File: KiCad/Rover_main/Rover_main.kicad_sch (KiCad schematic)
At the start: 50 parts, among them J1 ToF sensor header, J2 12v Regulator, J3 40 pin Nano header, J4 Motor 2, J5 Motor 1, J6 Motor 3, J7 Motor 4

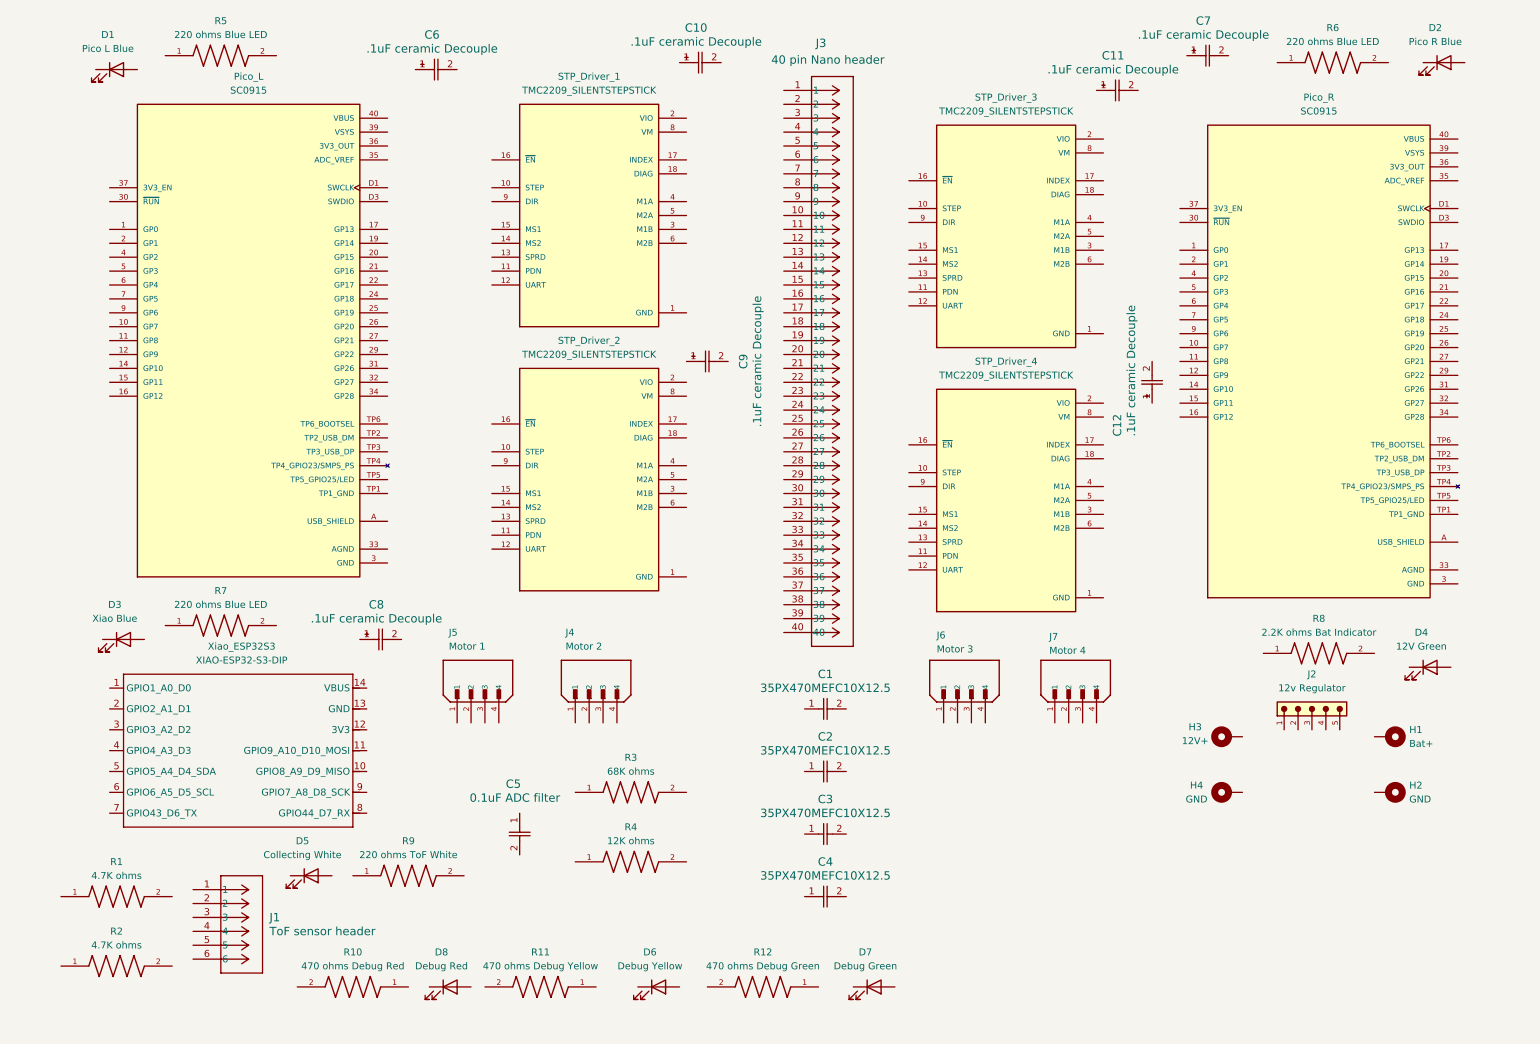
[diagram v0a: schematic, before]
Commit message: Updated KiCad Schematic
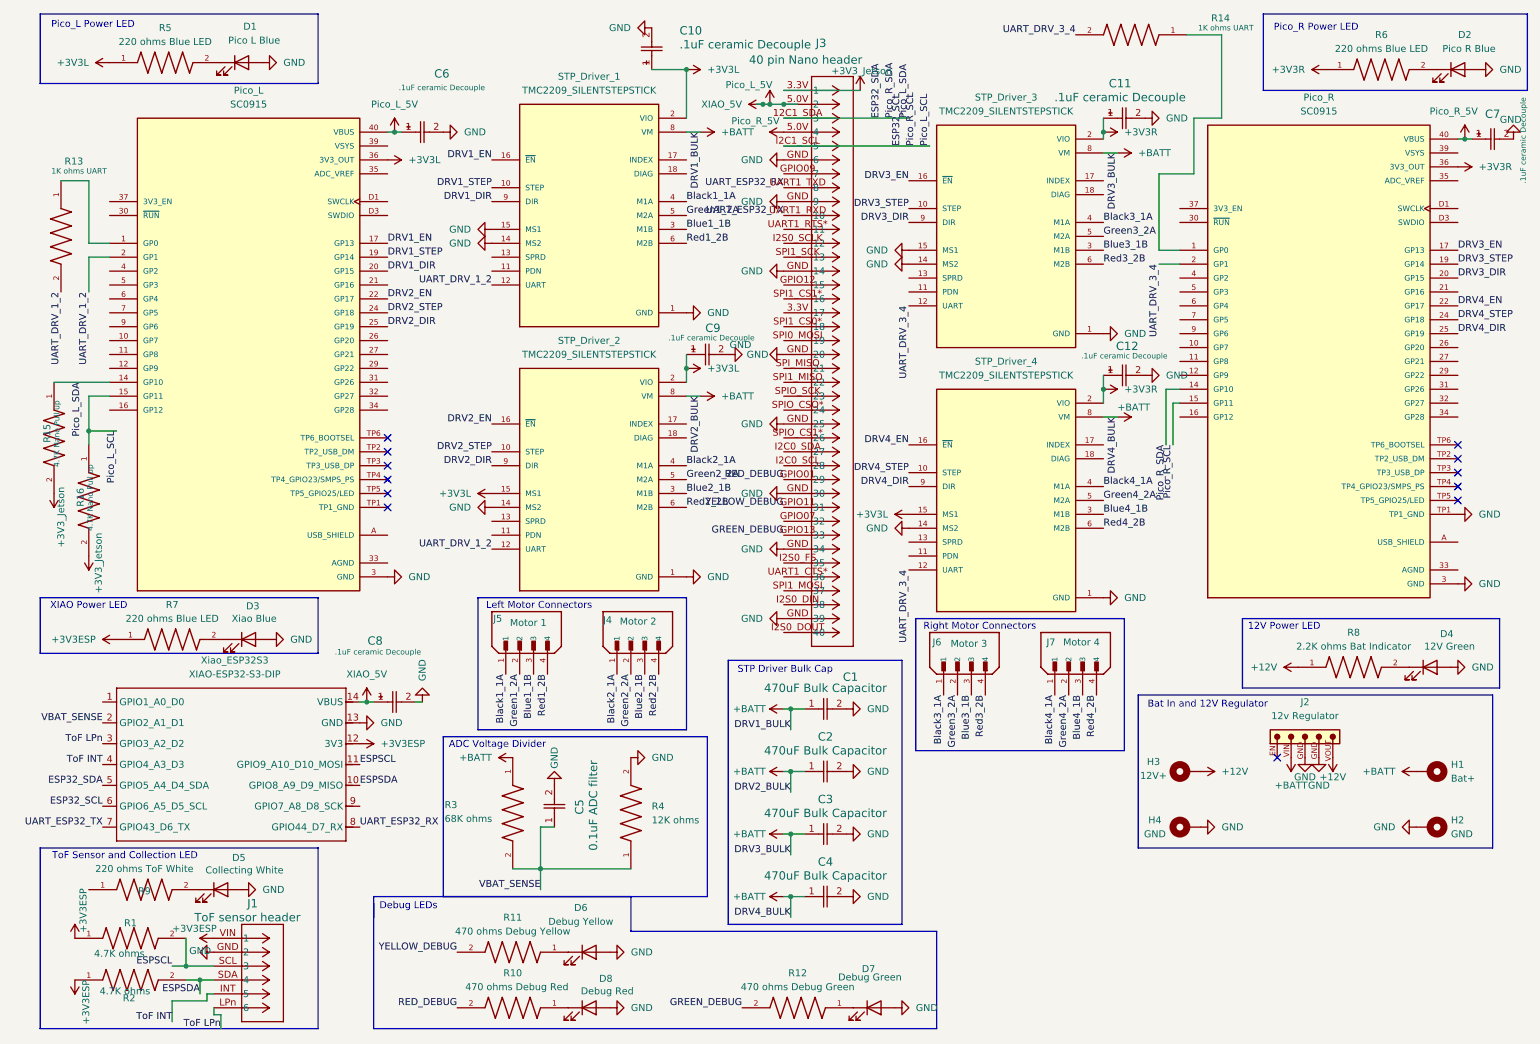
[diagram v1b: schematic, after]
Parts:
- added R13, R14: 1K ohms UART, RC1206FR-074K7L:RESC3116X65N, symbol New_Library:RC1206FR-074K7L
- added R15, R16: 4.7K Nano Pull up, RC1206FR-074K7L:RESC3116X65N, symbol New_Library:RC1206FR-074K7L
- C1, C2, C3, C4: value 35PX470MEFC10X12.5 -> 470uF Bulk Capacitor
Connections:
- net GND: now also C1.2, C10.2, C11.2, C12.2, C2.2, C3.2, C4.2, C5.2, C6.2, C7.2, C8.2, C9.2, D1.2 (A), D2.2 (A), D3.2 (A), D4.2 (A), D5.2 (A), D6.2 (A), D7.2 (A), D8.2 (A), H2.1, H4.1, J1.GND (2), J2.GND, J3.GND (39), Pico_R.TP1 (TP1_GND), R4.2, STP_Driver_1.14 (MS2), STP_Driver_1.15 (MS1), STP_Driver_2.14 (MS2), STP_Driver_3.14 (MS2), STP_Driver_3.15 (MS1), STP_Driver_4.14 (MS2), Xiao_ESP32S3.13 (GND)
- net at D5.1 (K): now also R9.2
- net at D7.1 (K): now also R12.1
- net +BATT: now reaches H1.1
- net +BATT: now also C1.1, C2.1, C3.1, C4.1, J2.VIN, R3.1, STP_Driver_1.8 (VM), STP_Driver_2.8 (VM), STP_Driver_3.8 (VM), STP_Driver_4.8 (VM)
- net VBAT_SENSE: now reaches R3.2
- net VBAT_SENSE: now also C5.1, R4.1, Xiao_ESP32S3.2 (GPIO2_A1_D1)
- net Black2_1A: now reaches J4.1
- net Black2_1A: now also STP_Driver_2.4 (M1A)
- net Green2_2A: now reaches J4.2
- net Green2_2A: now also STP_Driver_2.5 (M2A)
- net Blue2_1B: now reaches J4.3
- net Blue2_1B: now also STP_Driver_2.3 (M1B)
- net Red2_2B: now reaches J4.4
- net Red2_2B: now also STP_Driver_2.6 (M2B)
- net Black3_1A: now reaches J6.1
- net Black3_1A: now also STP_Driver_3.4 (M1A)
- net Green3_2A: now reaches J6.2
- net Green3_2A: now also STP_Driver_3.5 (M2A)
- net Blue3_1B: now reaches J6.3
- net Blue3_1B: now also STP_Driver_3.3 (M1B)
- net Red3_2B: now reaches J6.4
- net Red3_2B: now also STP_Driver_3.6 (M2B)
- net at D2.1 (K): now also R6.2
- net at Pico_R.1 (GP0): now also R14.1
- net ESP32_SDA: now reaches Pico_R.14 (GP10)
- net ESP32_SDA: now also J3.12C1_SDA (3), Pico_L.14 (GP10), Xiao_ESP32S3.5 (GPIO5_A4_D4_SDA), R15.1
- net ESP32_SCL: now reaches Pico_R.15 (GP11)
- net ESP32_SCL: now also J3.I2C1_SCL (5), Pico_L.15 (GP11), Xiao_ESP32S3.6 (GPIO6_A5_D5_SCL), R16.1
- net DRV3_EN: now reaches Pico_R.17 (GP13)
- net DRV3_EN: now also STP_Driver_3.16 (~{EN})
- net DRV3_STEP: now reaches Pico_R.19 (GP14)
- net DRV3_STEP: now also STP_Driver_3.10 (STEP)
- net UART_DRV_3_4: now reaches Pico_R.2 (GP1)
- net UART_DRV_3_4: now also STP_Driver_3.12 (UART), STP_Driver_4.12 (UART), R14.2
- net DRV3_DIR: now reaches Pico_R.20 (GP15)
- net DRV3_DIR: now also STP_Driver_3.9 (DIR)
- net DRV4_EN: now reaches Pico_R.22 (GP17)
- net DRV4_EN: now also STP_Driver_4.16 (~{EN})
- net DRV4_STEP: now reaches Pico_R.24 (GP18)
- net DRV4_STEP: now also STP_Driver_4.10 (STEP)
- net DRV4_DIR: now reaches Pico_R.25 (GP19)
- net DRV4_DIR: now also STP_Driver_4.9 (DIR)
- net +3V3R: now reaches Pico_R.36 (3V3_OUT)
- net +3V3R: now also C11.1, C12.1, R6.1, STP_Driver_3.2 (VIO), STP_Driver_4.2 (VIO)
- net Pico_R_5V: now reaches Pico_R.40 (VBUS)
- net Pico_R_5V: now also C7.1, J3.5.0V (4)
- net Black1_1A: now reaches J5.1
- net Black1_1A: now also STP_Driver_1.4 (M1A)
- net Green1_2A: now reaches J5.2
- net Green1_2A: now also STP_Driver_1.5 (M2A)
- net Blue1_1B: now reaches J5.3
- net Blue1_1B: now also STP_Driver_1.3 (M1B)
- net Red1_2B: now reaches J5.4
- net Red1_2B: now also STP_Driver_1.6 (M2B)
- net at D6.1 (K): now also R11.1
- net +3V3L: now reaches STP_Driver_4.15 (MS1)
- net +3V3L: now also C10.1, C9.1, Pico_L.36 (3V3_OUT), R5.1, STP_Driver_1.2 (VIO), STP_Driver_2.15 (MS1), STP_Driver_2.2 (VIO)
- net Blue4_1B: now reaches STP_Driver_4.3 (M1B)
- net Blue4_1B: now also J7.3
- net Black4_1A: now reaches STP_Driver_4.4 (M1A)
- net Black4_1A: now also J7.1
- net Green4_2A: now reaches STP_Driver_4.5 (M2A)
- net Green4_2A: now also J7.2
- net Red4_2B: now reaches STP_Driver_4.6 (M2B)
- net Red4_2B: now also J7.4
- net at D4.1 (K): now also R8.2
- net YELLOW_DEBUG: now reaches R11.2
- net YELLOW_DEBUG: now also J3.GPIO11 (31)
- net at D3.1 (K): now also R7.2
- net at D1.1 (K): now also R5.2
- net +3V3ESP: now reaches R7.1
- net +3V3ESP: now also J1.VIN (1), R1.1, R2.1, Xiao_ESP32S3.12 (3V3)
- net +12V: now reaches H3.1
- net +12V: now also J2.VOUT, R8.1
- net Pico_L_5V: now reaches C6.1
- net Pico_L_5V: now also C8.1, J3.5.0V (4), Pico_L.40 (VBUS), Xiao_ESP32S3.14 (VBUS)
- net ESPSDA: now reaches R2.2
- net ESPSDA: now also J1.SDA (4), Xiao_ESP32S3.10 (GPIO8_A9_D9_MISO)
- net DRV2_STEP: now reaches STP_Driver_2.10 (STEP)
- net DRV2_STEP: now also Pico_L.24 (GP18)
- net UART_DRV_1_2: now reaches STP_Driver_2.12 (UART)
- net UART_DRV_1_2: now also Pico_L.2 (GP1), STP_Driver_1.12 (UART), R13.2
- net DRV2_EN: now reaches STP_Driver_2.16 (~{EN})
- net DRV2_EN: now also Pico_L.22 (GP17)
- net DRV2_DIR: now reaches STP_Driver_2.9 (DIR)
- net DRV2_DIR: now also Pico_L.25 (GP19)
- net GREEN_DEBUG: now reaches R12.2
- net GREEN_DEBUG: now also J3.GPIO13 (33)
- net DRV1_STEP: now reaches STP_Driver_1.10 (STEP)
- net DRV1_STEP: now also Pico_L.19 (GP14)
- net DRV1_EN: now reaches STP_Driver_1.16 (~{EN})
- net DRV1_EN: now also Pico_L.17 (GP13)
- net DRV1_DIR: now reaches STP_Driver_1.9 (DIR)
- net DRV1_DIR: now also Pico_L.20 (GP15)
- net ESPSCL: now reaches R1.2
- net ESPSCL: now also J1.SCL (3), Xiao_ESP32S3.11 (GPIO9_A10_D10_MOSI)
- net at R10.1: now also D8.1 (K)
- net RED_DEBUG: now reaches R10.2
- net RED_DEBUG: now also J3.GPIO01 (29)
- net at Pico_L.1 (GP0): now also R13.1
- net ToF LPn: now reaches Xiao_ESP32S3.3 (GPIO3_A2_D2)
- net ToF LPn: now also J1.LPn (6)
- net ToF INT: now reaches Xiao_ESP32S3.4 (GPIO4_A3_D3)
- net ToF INT: now also J1.INT (5)
- net UART_ESP32_TX: now reaches Xiao_ESP32S3.7 (GPIO43_D6_TX)
- net UART_ESP32_TX: now also J3.UART1_RXD (10)
- net UART_ESP32_RX: now reaches Xiao_ESP32S3.8 (GPIO44_D7_RX)
- net UART_ESP32_RX: now also J3.UART1_TXD (8)
- new net +3V3_Jetson: J3.3.3V (17), R15.2, R16.2
- no-connect marks 0 -> 12
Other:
- note added: "12V Power LED"
- note added: "ADC Voltage Divider"
- note added: "Bat In and 12V Regulator"
- note added: "Debug LEDs"
- note added: "Left Motor Connectors"
- note added: "Pico_L Power LED"
- note added: "Pico_R Power LED"
- note added: "Right Motor Connectors"
- note added: "STP Driver Bulk Cap"
- note added: "ToF Sensor and Collection LED"
- note added: "XIAO Power LED"
- moved on the sheet: C10, C11, C12, C5, C6, C7, C8, C9, D1, D2, D3, D5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
